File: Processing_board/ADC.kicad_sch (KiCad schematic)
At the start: 61 parts, among them U10 ADS1299IPAG, U11 ADS1299IPAG

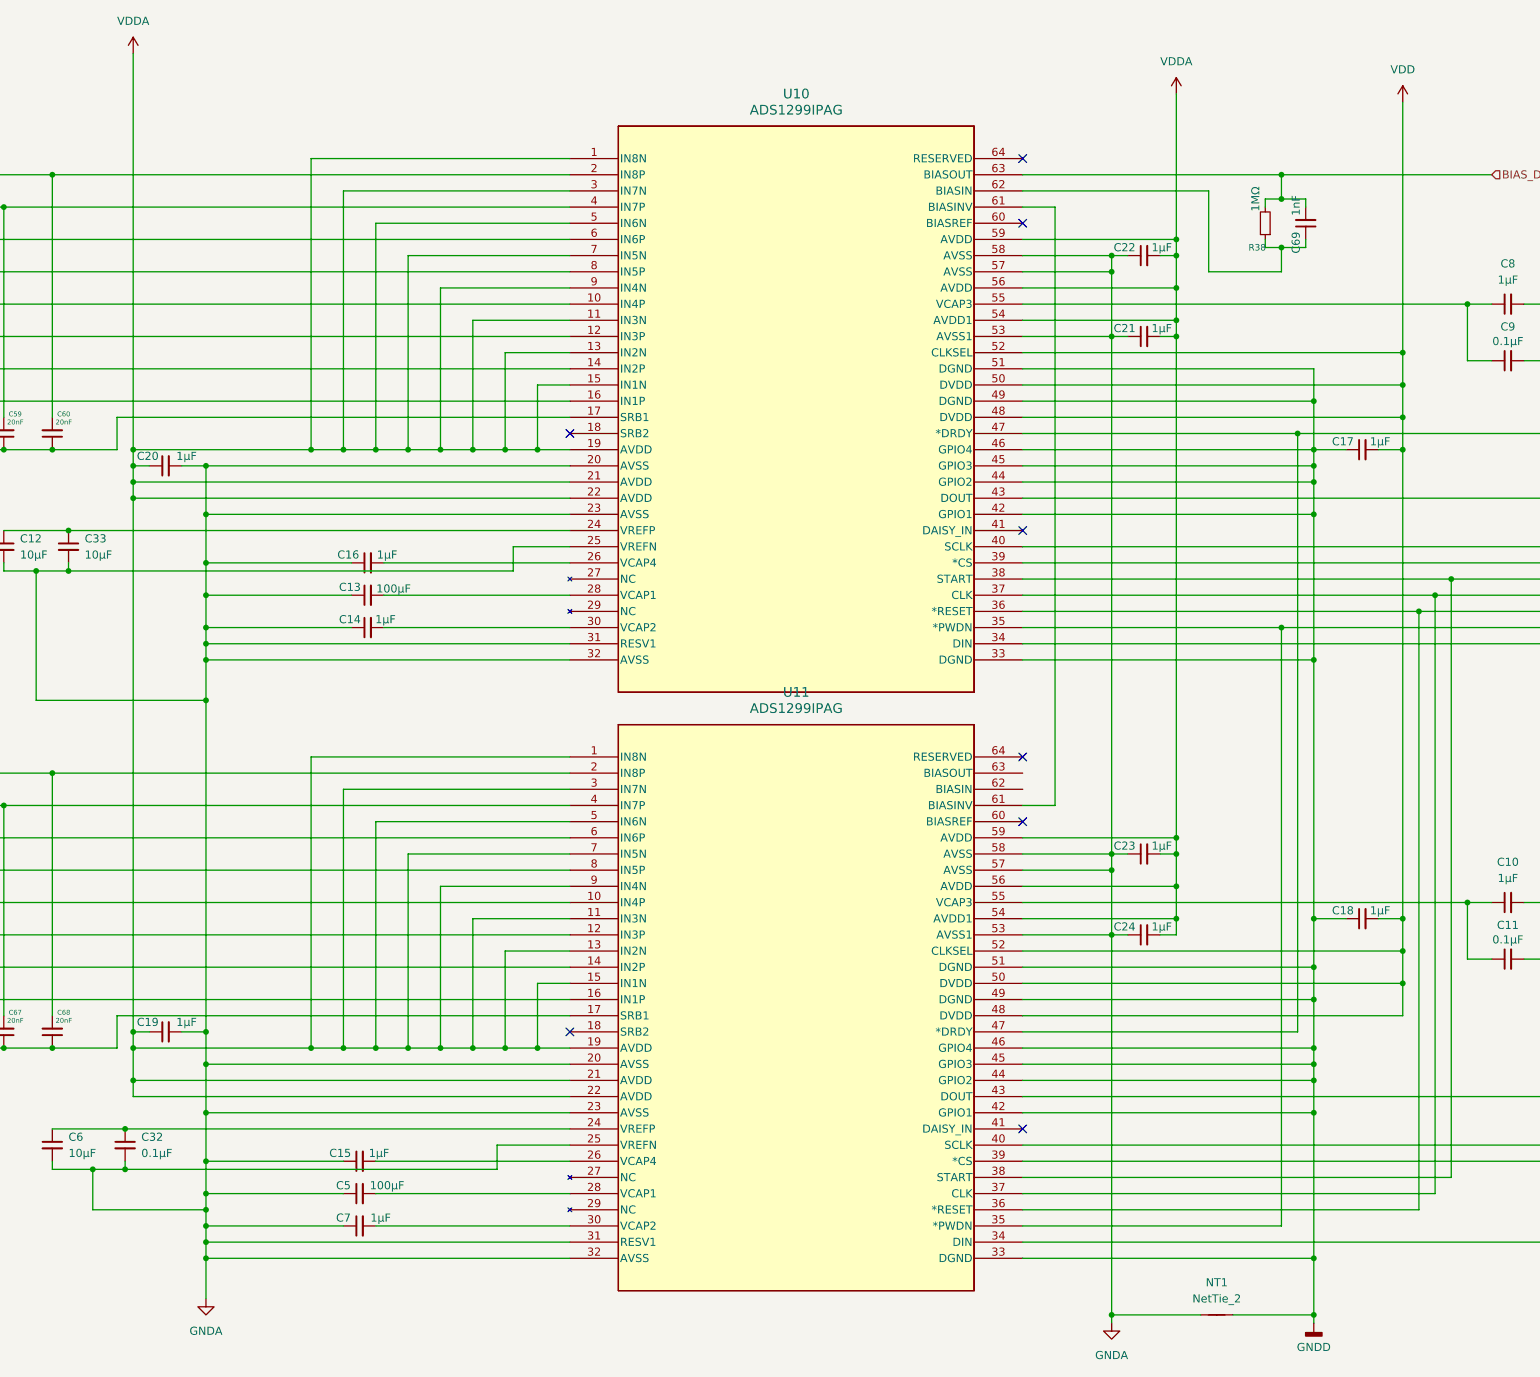
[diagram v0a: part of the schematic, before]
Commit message: Add the new power supply and connect the ADCs at the GND an power
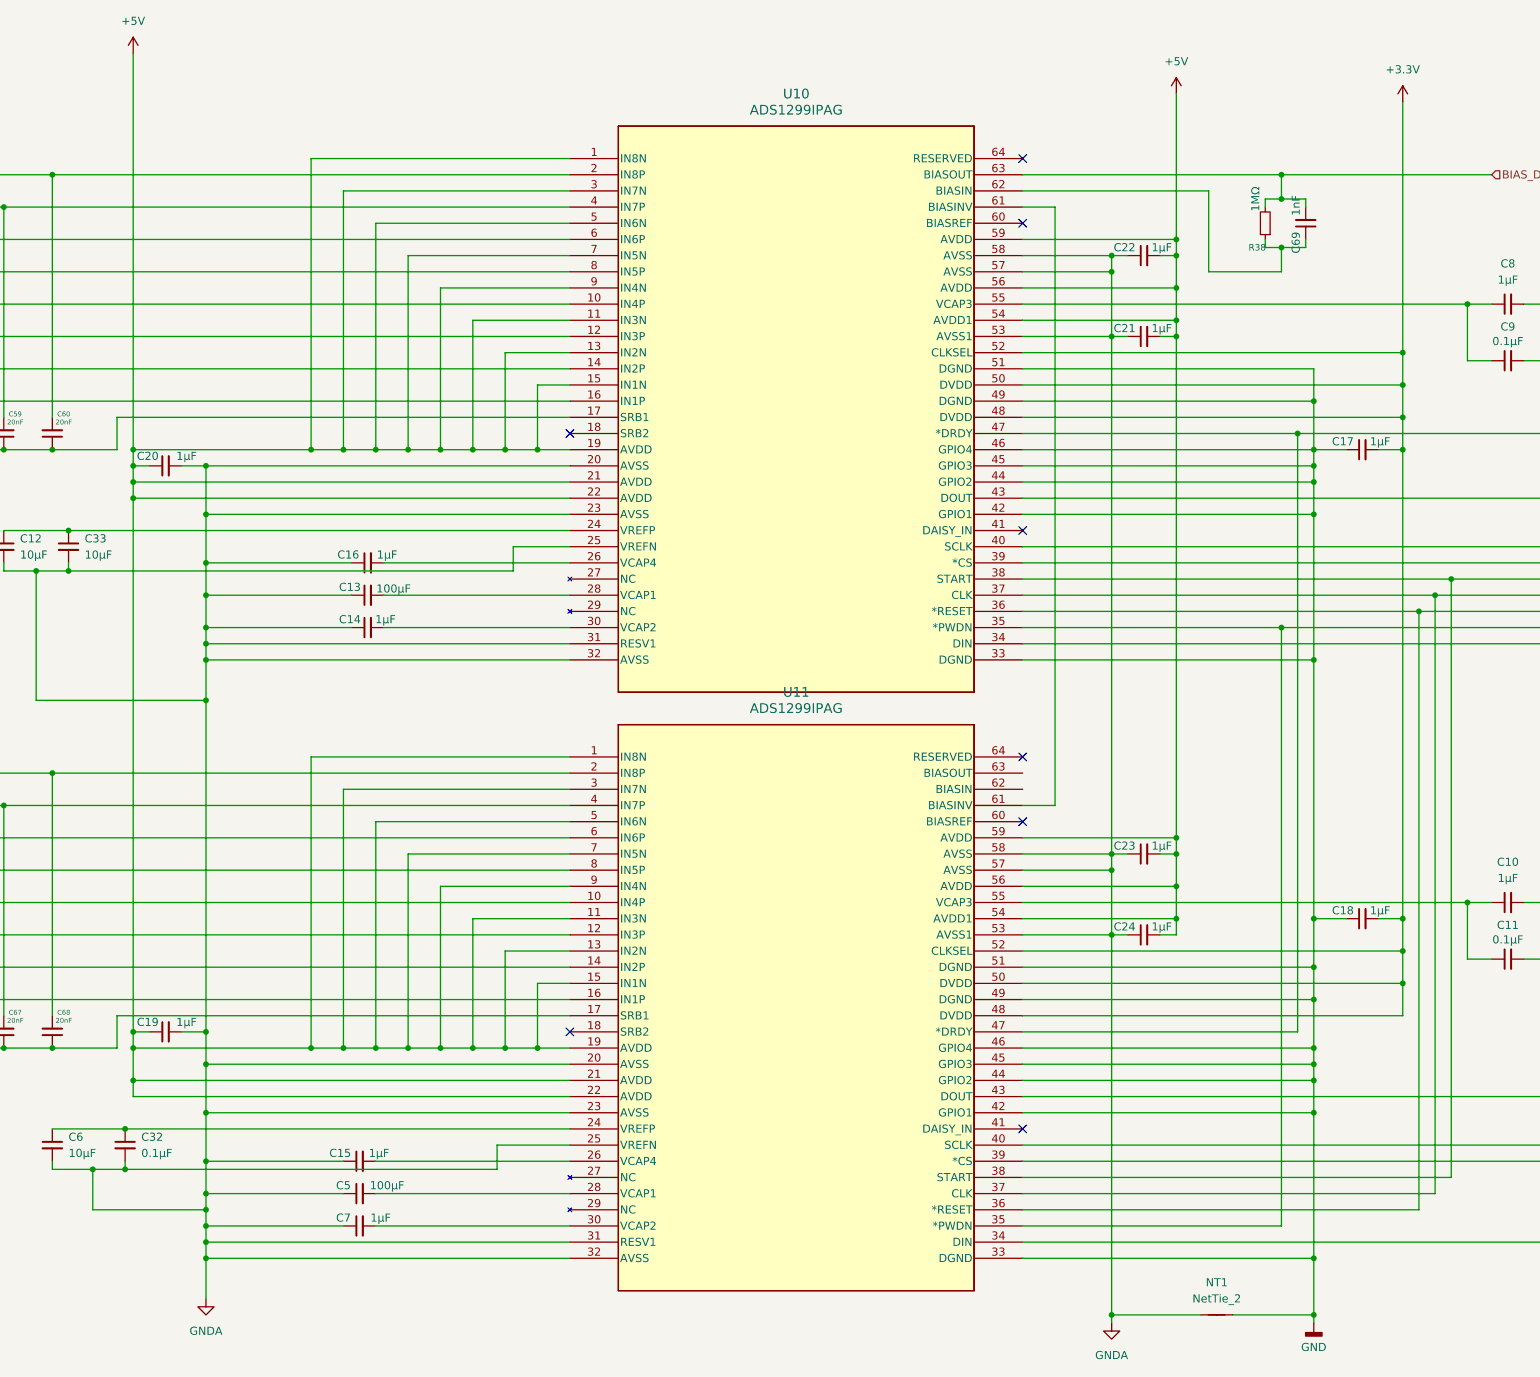
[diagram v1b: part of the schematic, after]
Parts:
- NT1: footprint (none) -> NetTie:NetTie-2_SMD_Pad0.5mm
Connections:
- net GNDD renamed GND
- net VDD renamed +3.3V
- net VDDA renamed +5V
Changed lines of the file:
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@@
 			)
 		)
-		(property "Value" "VDDA"
+		(property "Value" "+5V"
 			(at 139.7 36.83 0)
 			(effects
@@
 			)
 		)
-		(property "Description" "Power symbol creates a global label with name \"VDDA\""
+		(property "Description" "Power symbol creates a global label with name \"+5V\""
 			(at 139.7 41.91 0)
 			(effects
@@
 			)
 		)
-		(property "Value" "GNDD"
+		(property "Value" "GND"
 			(at 325.12 245.11 0)
 			(effects
@@
 			)
 		)
-		(property "Description" "Power symbol creates a global label with name \"GNDD\" , digital ground"
+		(property "Description" "Power symbol creates a global label with name \"GND\" , digital ground"
 			(at 325.12 241.3 0)
 			(effects
@@
 			)
 		)
-		(property "Value" "VDDA"
+		(property "Value" "+5V"
 			(at 303.53 43.18 0)
 			(effects
@@
 			)
 		)
-		(property "Description" "Power symbol creates a global label with name \"VDDA\""
+		(property "Description" "Power symbol creates a global label with name \"+5V\""
 			(at 303.53 48.26 0)
 			(effects
@@
 			)
 		)
-		(property "Footprint" ""
+		(property "Footprint" "NetTie:NetTie-2_SMD_Pad0.5mm"
 			(at 309.88 240.03 0)
 			(effects
@@
 			)
 		)
-		(property "Value" "VDD"
+		(property "Value" "+3.3V"
 			(at 339.09 44.45 0)
 			(effects
@@
 			)
 		)
-		(property "Description" "Power symbol creates a global label with name \"VDD\""
+		(property "Description" "Power symbol creates a global label with name \"+3.3V\""
 			(at 339.09 49.53 0)
 			(effects
